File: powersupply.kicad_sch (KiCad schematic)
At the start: 33 parts, among them U2 MP28167GQ, U3 PAM2306AYPKE

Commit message: Label RasPi Zero W pin header
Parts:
- added D1: LED, LED_SMD:LED_0805_2012Metric, symbol Device:LED
- added J1: 2477, 2477, symbol STS1_EEE_lib:2477
- added R1: 220, Resistor_SMD:R_0603_1608Metric, symbol Device:R
- added SW1: SW_SPST, symbol Switch:SW_SPST
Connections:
- net AGND: now also D1.1 (K), J1.2 (-)
- net VBUS: now also R1.1, SW1.2 (B)
- new net: D1.2 (A), R1.2
- new net: J1.1 (+), SW1.1 (A)

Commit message: Add 3V3 LDO: could be used to set EPS_BAT_GOOD high
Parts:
- removed C17: 100n, Capacitor_SMD:C_0603_1608Metric_Pad1.08x0.95mm_HandSolder, symbol STS1_EDU-rescue:C-Device-STS1_template-rescue
- removed C18, C19, C20, C21: 10u, Capacitor_SMD:C_0603_1608Metric_Pad1.08x0.95mm_HandSolder, symbol STS1_EDU-rescue:C-Device-STS1_template-rescue
- removed L2, L3: 4.7uH, Inductor_SMD:L_1210_3225Metric_Pad1.42x2.65mm_HandSolder, symbol STS1_EDU-rescue:L-Device-STS1_template-rescue
- removed R13: 100k, Resistor_SMD:R_0603_1608Metric_Pad0.98x0.95mm_HandSolder, symbol STS1_EDU-rescue:R-Device-STS1_template-rescue
- removed TP1, TP2: TestPoint, TestPoint:TestPoint_Pad_1.0x1.0mm, symbol Connector:TestPoint
- removed U3: PAM2306AYPKE, PAM2306AYPKE:SON45P300X300X80-13N, symbol PAM2306AYPKE:PAM2306AYPKE
- added C13: 4.7u, Capacitor_SMD:C_0603_1608Metric, symbol Device:C
- added D23: PTVS3V3S1UR,115, Diode_SMD:D_SOD-123, symbol Device:D_Zener
- added U4: MCP1725-3302E_MC, STS1_3V3:MCP1725-3302E&slash_MC, symbol STS1_3V3:MCP1725-3302E_MC
- SW1: footprint (none) -> Button_Switch_THT:SW_DIP_SPSTx01_Slide_9.78x4.72mm_W7.62mm_P2.54mm
- renumbered C5 to C1, C14 to C10, C15 to C11, C16 to C12, C6 to C2, C7 to C3, C8 to C4, C9 to C5, C10 to C6, C11 to C7, C12 to C8, C13 to C9, D3 to D1, D4 to D2, D1 to D3, D5 to D4, D6 to D5, J1 to J3, R11 to R1, R12 to R2, R1 to R3, R14 to R4, R15 to R5, U2 to U3
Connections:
- net 3V3: now also C13.2, D23.1 (K), U4.7 (SENSE), U4.8 (VOUT)
- net AGND: now also C13.1, D23.2 (A), U4.4 (GND), U4.9 (EP)
- net VBUS: now also U4.1 (VIN), U4.2 (VIN), U4.3 (*SHDN)
- no-connect marks 0 -> 2
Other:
- note removed: "Step Down 5V --> 3V3 ^ 1V8"
- moved on the sheet: D3, J3, R3, SW1

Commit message: Clean-up
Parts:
- U4: footprint STS1_3V3:MCP1725-3302E&slash_MC -> STS_EEE:MCP1725-3302E&slash_MC
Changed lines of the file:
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@@
 			)
 		)
-		(property "Footprint" "STS1_3V3:MCP1725-3302E&slash_MC"
+		(property "Footprint" "STS_EEE:MCP1725-3302E&slash_MC"
 			(at 95.25 118.364 0)
 			(hide yes)

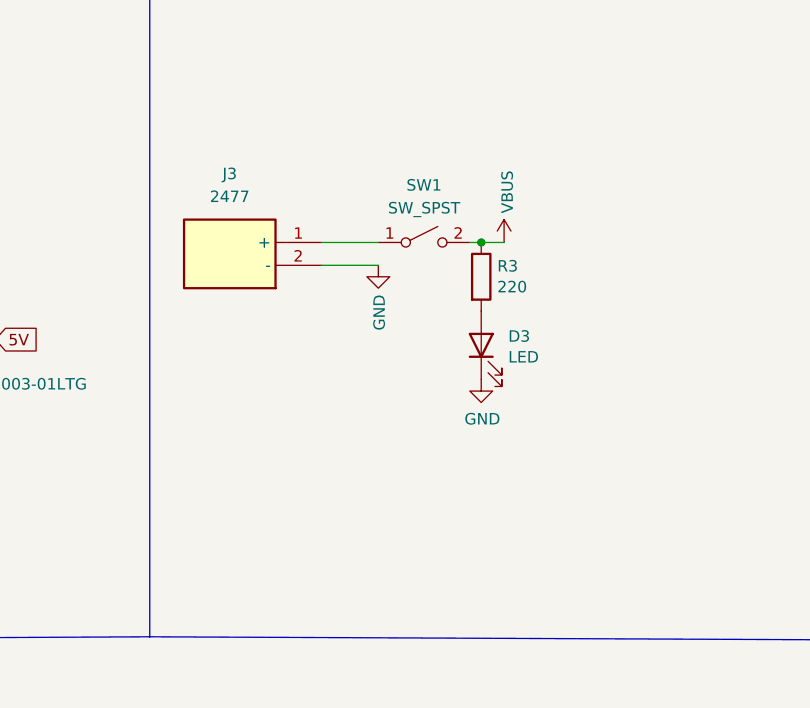
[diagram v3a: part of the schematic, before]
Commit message: Replace AA battery holder with 18650 one
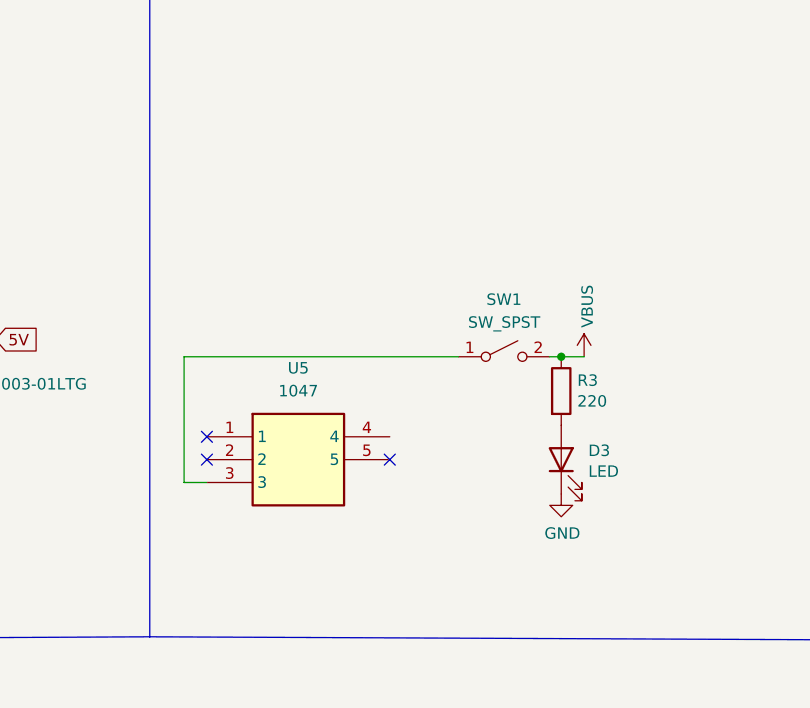
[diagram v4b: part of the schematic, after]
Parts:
- removed J3: 2477, 2477, symbol STS1_EEE_lib:2477
- added U5: 1047, 1047, symbol 1047:1047
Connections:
- net at SW1.1 (A): now also U5.3
- no-connect marks 2 -> 5
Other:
- moved on the sheet: D3, R3, SW1

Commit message: Position PiHat, Raspberry Zero, and battery holder
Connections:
- net 5V is gone; now on net VBUS: C10.1, C11.1, C12.1, C9.1, D2.1 (K), R5.1, U3.12 (OUT)
- net AGND: now also U5.4
- net VBUS: no longer C1.1, C2.1, C3.1, D1.1 (K), R1.1, R3.1, SW1.2 (B), U3.1 (IN)
- new net VBAT: C1.1, C2.1, C3.1, D1.1 (K), R1.1, R3.1, SW1.2 (B), U3.1 (IN)
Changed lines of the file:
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@@
 	(wire
 		(pts
+			(xy 294.64 64.77) (xy 289.56 64.77)
+		)
+		(stroke
+			(width 0)
+			(type default)
+		)
+	)
+	(wire
+		(pts
 			(xy 138.43 127) (xy 146.05 127)
 		)
@@
 	(wire
 		(pts
+			(xy 294.64 71.12) (xy 294.64 64.77)
+		)
+		(stroke
+			(width 0)
+			(type default)
+		)
+	)
+	(wire
+		(pts
 			(xy 120.65 127) (xy 123.19 127)
 		)
@@
 		)
 	)
-	(global_label "VBUS"
+	(global_label "VBAT"
 		(shape input)
 		(at 34.925 32.385 180)
@@
 		)
 		(property "Intersheetrefs" "${INTERSHEET_REFS}"
-			(at 27.7022 32.4644 0)
+			(at 28.1792 32.385 0)
 			(hide yes)
 			(show_name no)
@@
 		)
 	)
-	(global_label "5V"
+	(global_label "VBUS"
 		(shape input)
-		(at 389.255 106.68 90)
+		(at 63.5 124.46 180)
 		(fields_autoplaced yes)
 		(effects
@@
 				(size 1.27 1.27)
 			)
-			(justify left)
+			(justify right)
 		)
 		(property "Intersheetrefs" "${INTERSHEET_REFS}"
-			(at 389.1756 102.0577 90)
+			(at 56.2704 124.46 0)
 			(hide yes)
 			(show_name no)
@@
 					(size 1.27 1.27)
 				)
-				(justify left)
+				(justify right)
 			)
 		)
 	)
-	(global_label "3V3"
+	(global_label "VBUS"
 		(shape input)
-		(at 158.75 127 0)
+		(at 389.255 106.68 90)
 		(fields_autoplaced yes)
 		(effects
@@
 		)
 		(property "Intersheetrefs" "${INTERSHEET_REFS}"
-			(at 164.5886 127 0)
+			(at 389.255 99.4504 90)
 			(hide yes)
 			(show_name no)
@@
 		)
 	)
-	(global_label "5V"
+	(global_label "3V3"
 		(shape input)
-		(at 245.745 53.975 0)
+		(at 158.75 127 0)
 		(fields_autoplaced yes)
 		(effects
@@
 		)
 		(property "Intersheetrefs" "${INTERSHEET_REFS}"
-			(at 250.3673 53.8956 0)
+			(at 164.5886 127 0)
 			(hide yes)
 			(show_name no)
@@
 		)
 	)
-	(hierarchical_label "VBUS"
+	(global_label "VBUS"
 		(shape input)
-		(at 63.5 124.46 180)
+		(at 245.745 53.975 0)
+		(fields_autoplaced yes)
 		(effects
 			(font
 				(size 1.27 1.27)
 			)
-			(justify right)
+			(justify left)
+		)
+		(property "Intersheetrefs" "${INTERSHEET_REFS}"
+			(at 252.9746 53.975 0)
+			(hide yes)
+			(show_name no)
+			(do_not_autoplace no)
+			(effects
+				(font
+					(size 1.27 1.27)
+				)
+				(justify left)
+			)
 		)
 	)
@@
 	(symbol
 		(lib_id "power:GND")
+		(at 294.64 71.12 0)
+		(unit 1)
+		(body_style 1)
+		(exclude_from_sim no)
+		(in_bom yes)
+		(on_board yes)
+		(in_pos_files yes)
+		(dnp no)
+		(property "Reference" "#PWR053"
+			(at 294.64 77.47 0)
+			(hide yes)
+			(show_name no)
+			(do_not_autoplace no)
+			(effects
+				(font
+					(size 1.27 1.27)
+				)
+			)
+		)
+		(property "Value" "GND"
+			(at 294.767 75.5142 0)
+			(show_name no)
+			(do_not_autoplace no)
+			(effects
+				(font
+					(size 1.27 1.27)
+				)
+			)
+		)
+		(property "Footprint" ""
+			(at 294.64 71.12 0)
+			(hide yes)
+			(show_name no)
+			(do_not_autoplace no)
+			(effects
+				(font
+					(size 1.27 1.27)
+				)
+			)
+		)
+		(property "Datasheet" ""
+			(at 294.64 71.12 0)
+			(hide yes)
+			(show_name no)
+			(do_not_autoplace no)
+			(effects
+				(font
+					(size 1.27 1.27)
+				)
+			)
+		)
+		(property "Description" ""
+			(at 294.64 71.12 0)
+			(show_name no)
+			(do_not_autoplace no)
+			(effects
+				(font
+					(size 1.27 1.27)
+				)
+			)
+		)
+		(pin "1"
+		)
+		(instances
+			(project "STS1_EEE"
+				(path "/81e05c2b-9a2c-430f-84ee-6a59968cd49a/f7af00b0-76c3-459f-8c46-f5a83dd3bee8"
+					(reference "#PWR053")
+					(unit 1)
+				)
+			)
+		)
+	)
+	(symbol
+		(lib_id "power:GND")
 		(at 227.965 62.865 0)
 		(unit 1)
@@
 			)
 		)
-		(property "Value" "VBUS"
+		(property "Value" "VBAT"
 			(at 311.531 52.6542 90)
 			(show_name no)

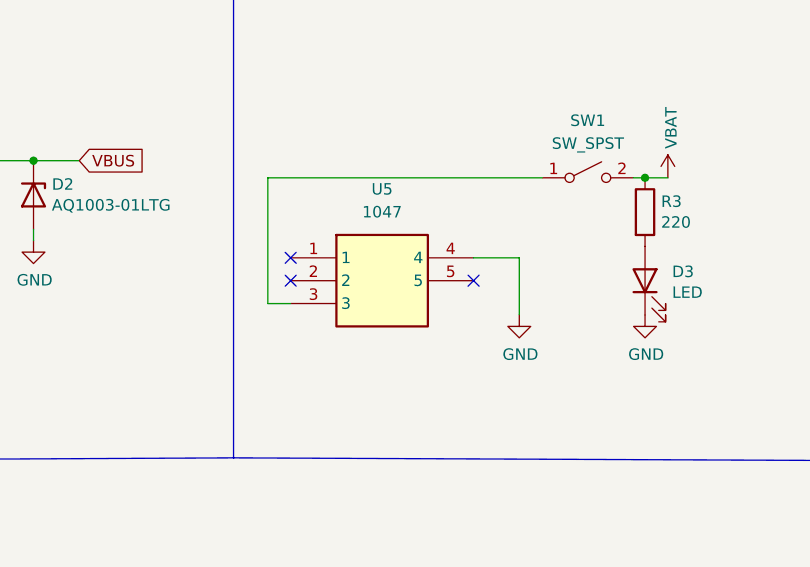
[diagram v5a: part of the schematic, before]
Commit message: Replace 1047 battery holder with 1048P (battery contacts connect to PCB using pads)
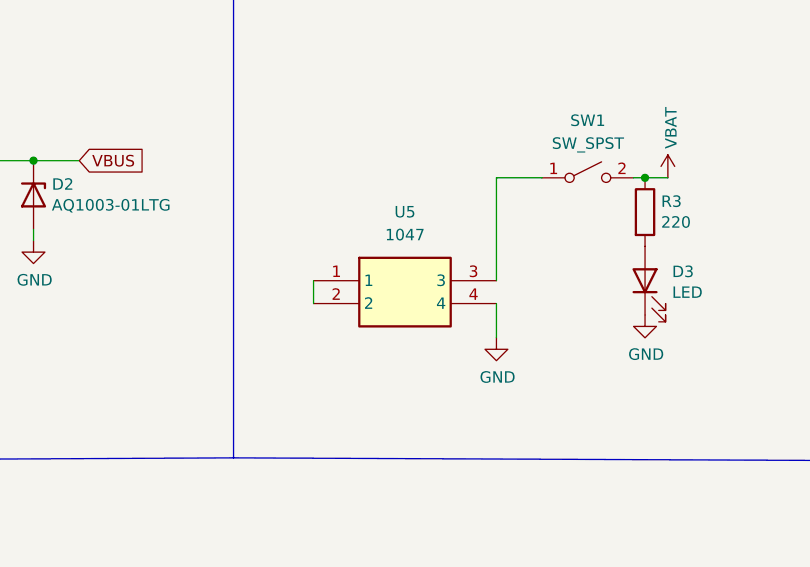
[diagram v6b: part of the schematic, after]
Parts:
- U5: footprint 1047 -> 1048P; symbol 1047:1047 -> STS1_EEE_lib:1048P; Manufacturer_Part_Number 1047 -> 1048P; Mouser Part Number 534-1047 -> 534-1048P; Mouser Price/Stock https://www.mouser.co.uk/ProductDetail/Keystone-Electronics/1047?qs=up89fPMRNqBQruBm7zqCRQ%3D%3D -> https://www.mouser.co.uk/ProductDetail/Keystone-Electronics/1048P?qs=9%252Bwcgl%2FJqd1h8Vx3IFpTxA%3D%3D
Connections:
- net at U5.1: now also U5.2
- no-connect marks 5 -> 2
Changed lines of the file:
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@@
 	)
 	(no_connect
-		(at 289.56 67.31)
-	)
-	(no_connect
 		(at 120.65 134.62)
 	)
 	(no_connect
-		(at 269.24 67.31)
-	)
-	(no_connect
 		(at 120.65 132.08)
 	)
-	(no_connect
-		(at 269.24 64.77)
-	)
 	(wire
 		(pts
@@
 	(wire
 		(pts
-			(xy 269.24 69.85) (xy 266.7 69.85)
-		)
-		(stroke
-			(width 0)
-			(type default)
-		)
-	)
-	(wire
-		(pts
 			(xy 205.105 62.865) (xy 205.105 61.595)
 		)
@@
 	(wire
 		(pts
-			(xy 266.7 55.88) (xy 297.18 55.88)
-		)
-		(stroke
-			(width 0)
-			(type default)
-		)
-	)
-	(wire
-		(pts
 			(xy 216.535 53.975) (xy 227.965 53.975)
 		)
@@
 	(wire
 		(pts
-			(xy 180.975 32.385) (xy 180.975 37.465)
+			(xy 292.1 69.85) (xy 292.1 73.66)
 		)
 		(stroke
@@
 	(wire
 		(pts
-			(xy 389.255 129.54) (xy 389.255 132.08)
+			(xy 180.975 32.385) (xy 180.975 37.465)
 		)
 		(stroke
@@
 	(wire
 		(pts
-			(xy 120.65 124.46) (xy 125.73 124.46)
+			(xy 389.255 129.54) (xy 389.255 132.08)
 		)
 		(stroke
@@
 	(wire
 		(pts
-			(xy 94.615 32.385) (xy 130.175 32.385)
+			(xy 120.65 124.46) (xy 125.73 124.46)
 		)
 		(stroke
@@
 	(wire
 		(pts
-			(xy 266.7 69.85) (xy 266.7 55.88)
+			(xy 94.615 32.385) (xy 130.175 32.385)
 		)
 		(stroke
@@
 	(wire
 		(pts
+			(xy 292.1 55.88) (xy 297.18 55.88)
+		)
+		(stroke
+			(width 0)
+			(type default)
+		)
+	)
+	(wire
+		(pts
 			(xy 63.5 124.46) (xy 67.31 124.46)
 		)
@@
 	(wire
 		(pts
+			(xy 292.1 55.88) (xy 292.1 67.31)
+		)
+		(stroke
+			(width 0)
+			(type default)
+		)
+	)
+	(wire
+		(pts
 			(xy 120.015 46.355) (xy 130.175 46.355)
 		)
@@
 	(wire
 		(pts
-			(xy 294.64 64.77) (xy 289.56 64.77)
+			(xy 138.43 127) (xy 146.05 127)
 		)
 		(stroke
@@
 	(wire
 		(pts
-			(xy 138.43 127) (xy 146.05 127)
+			(xy 170.815 37.465) (xy 180.975 37.465)
 		)
 		(stroke
@@
 	(wire
 		(pts
-			(xy 170.815 37.465) (xy 180.975 37.465)
+			(xy 307.34 55.88) (xy 308.61 55.88)
 		)
 		(stroke
@@
 	(wire
 		(pts
-			(xy 307.34 55.88) (xy 308.61 55.88)
+			(xy 130.175 67.945) (xy 130.175 59.055)
 		)
 		(stroke
@@
 	(wire
 		(pts
-			(xy 130.175 67.945) (xy 130.175 59.055)
+			(xy 216.535 62.865) (xy 216.535 61.595)
 		)
 		(stroke
@@
 	(wire
 		(pts
-			(xy 216.535 62.865) (xy 216.535 61.595)
+			(xy 170.815 60.325) (xy 170.815 62.865)
 		)
 		(stroke
@@
 	(wire
 		(pts
-			(xy 170.815 60.325) (xy 170.815 62.865)
+			(xy 271.78 67.31) (xy 271.78 69.85)
 		)
 		(stroke
@@
 	(wire
 		(pts
-			(xy 294.64 71.12) (xy 294.64 64.77)
-		)
-		(stroke
-			(width 0)
-			(type default)
-		)
-	)
-	(wire
-		(pts
 			(xy 120.65 127) (xy 123.19 127)
 		)
@@
 	(symbol
 		(lib_id "power:GND")
-		(at 294.64 71.12 0)
+		(at 292.1 73.66 0)
 		(unit 1)
 		(body_style 1)
@@
 		(dnp no)
 		(property "Reference" "#PWR053"
-			(at 294.64 77.47 0)
+			(at 292.1 80.01 0)
 			(hide yes)
 			(show_name no)
@@
 		)
 		(property "Value" "GND"
-			(at 294.767 75.5142 0)
+			(at 292.227 78.0542 0)
 			(show_name no)
 			(do_not_autoplace no)
@@
 		)
 		(property "Footprint" ""
-			(at 294.64 71.12 0)
+			(at 292.1 73.66 0)
 			(hide yes)
 			(show_name no)
@@
 		)
 		(property "Datasheet" ""
-			(at 294.64 71.12 0)
+			(at 292.1 73.66 0)
 			(hide yes)
 			(show_name no)
@@
 		)
 		(property "Description" ""
-			(at 294.64 71.12 0)
+			(at 292.1 73.66 0)
 			(show_name no)
 			(do_not_autoplace no)
@@
 	)
 	(symbol
-		(lib_id "1047:1047")
-		(at 269.24 64.77 0)
+		(lib_id "STS1_EEE_lib:1048P")
+		(at 271.78 67.31 0)
 		(unit 1)
 		(body_style 1)
@@
 		(fields_autoplaced yes)
 		(property "Reference" "U5"
-			(at 279.4 57.15 0)
+			(at 281.94 59.69 0)
 			(show_name no)
 			(do_not_autoplace no)
@@
 		)
 		(property "Value" "1047"
-			(at 279.4 59.69 0)
+			(at 281.94 62.23 0)
 			(show_name no)
 			(do_not_autoplace no)
@@
 			)
 		)
-		(property "Footprint" "1047"
-			(at 285.75 159.69 0)
+		(property "Footprint" "1048P"
+			(at 288.29 162.23 0)
 			(hide yes)
 			(show_name no)
@@
 			)
 		)
-		(property "Datasheet" "https://www.keyelco.com/product.cfm/product_id/14061"
-			(at 285.75 259.69 0)
+		(property "Datasheet" "http://www.keyelco.com/product-pdf.cfm?p=13959"
+			(at 288.29 262.23 0)
 			(hide yes)
 			(show_name no)
@@
 			)
 		)
-		(property "Description" "KEYSTONE - 1047 - BATTERY HOLDER, 18650 LI-ION, 2CELL, PCB"
-			(at 269.24 64.77 0)
+		(property "Description" "KEYSTONE - 1048P - BATTERY HOLDER, 18650, SMD"
+			(at 271.78 67.31 0)
 			(hide yes)
 			(show_name no)
@@
 		)
 		(property "Height" "14.85"
-			(at 285.75 459.69 0)
+			(at 288.29 462.23 0)
 			(hide yes)
 			(show_name no)
@@
 			)
 		)
-		(property "Mouser Part Number" "534-1047"
-			(at 285.75 559.69 0)
+		(property "Mouser Part Number" "534-1048P"
+			(at 288.29 562.23 0)
 			(hide yes)
 			(show_name no)
@@
 			)
 		)
-		(property "Mouser Price/Stock" "https://www.mouser.co.uk/ProductDetail/Keystone-Electronics/1047?qs=up89fPMRNqBQruBm7zqCRQ%3D%3D"
-			(at 285.75 659.69 0)
+		(property "Mouser Price/Stock" "https://www.mouser.co.uk/ProductDetail/Keystone-Electronics/1048P?qs=9%252Bwcgl%2FJqd1h8Vx3IFpTxA%3D%3D"
+			(at 288.29 662.23 0)
 			(hide yes)
 			(show_name no)
@@
 		)
 		(property "Manufacturer_Name" "Keystone Electronics"
-			(at 285.75 759.69 0)
+			(at 288.29 762.23 0)
 			(hide yes)
 			(show_name no)
@@
 			)
 		)
-		(property "Manufacturer_Part_Number" "1047"
-			(at 285.75 859.69 0)
+		(property "Manufacturer_Part_Number" "1048P"
+			(at 288.29 862.23 0)
 			(hide yes)
 			(show_name no)
@@
 			)
 		)
-		(pin "5"
-		)
 		(pin "4"

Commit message: Finilize connection and placement of components
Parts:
- removed C13: 4.7u, Capacitor_SMD:C_0603_1608Metric, symbol Device:C
- removed D23: PTVS3V3S1UR,115, Diode_SMD:D_SOD-123, symbol Device:D_Zener
- removed D3: LED, LED_SMD:LED_0805_2012Metric, symbol Device:LED
- removed R3: 220, Resistor_SMD:R_0603_1608Metric, symbol Device:R
- removed U4: MCP1725-3302E_MC, STS_EEE:MCP1725-3302E&slash_MC, symbol STS1_3V3:MCP1725-3302E_MC
- U4: renamed from U5; footprint 1048P -> STS_EEE:1048P
- renumbered D4 to D3, D5 to D4, R4 to R3, R5 to R4
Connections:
- net 3V3 renamed Pi_3V3
- no-connect marks 2 -> 0
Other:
- note added: "Battery power switch"
- note added: "Step Down VBAT --> VBUS 5V"
- note removed: "Step Down VBUS --> 5V"
- moved on the sheet: D3, D4, R3, R4, SW1, U4

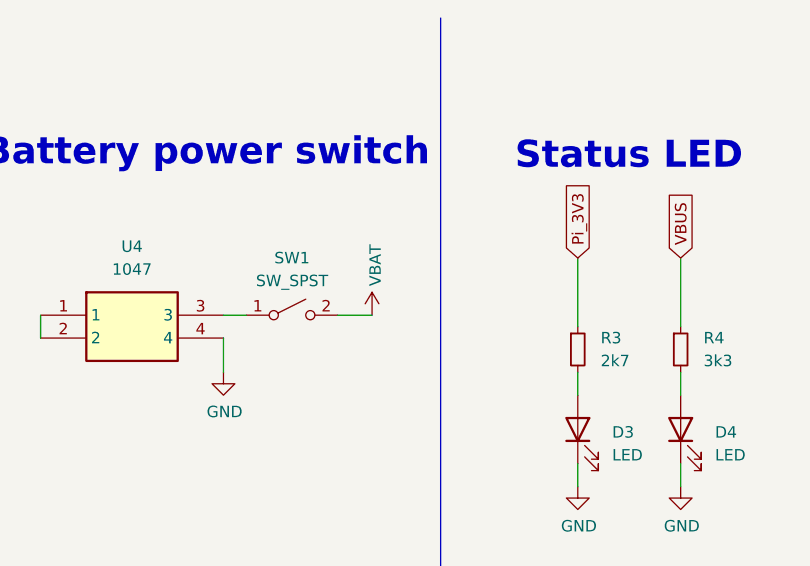
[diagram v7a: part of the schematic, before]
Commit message: Fix ERC errors
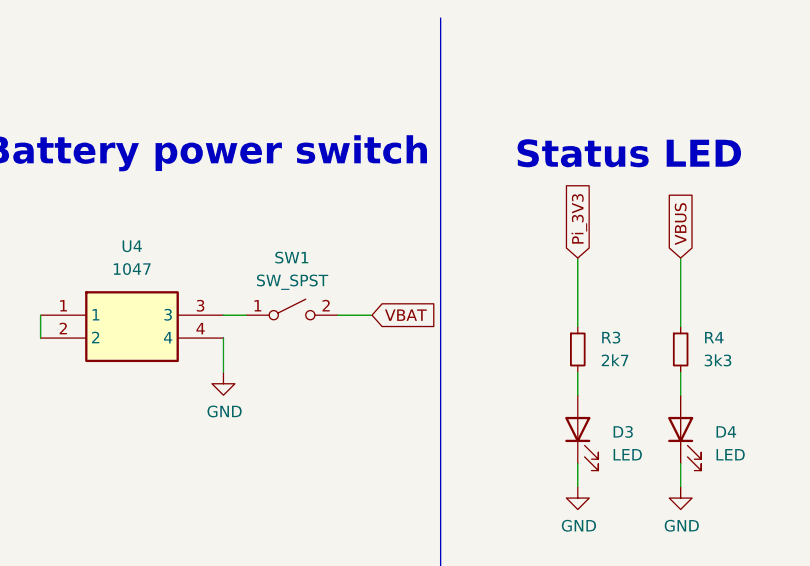
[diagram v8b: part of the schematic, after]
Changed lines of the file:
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@@
 		)
 	)
+	(global_label "VBAT"
+		(shape input)
+		(at 309.88 45.72 0)
+		(fields_autoplaced yes)
+		(effects
+			(font
+				(size 1.27 1.27)
+			)
+			(justify left)
+		)
+		(property "Intersheetrefs" "${INTERSHEET_REFS}"
+			(at 316.6258 45.72 0)
+			(hide yes)
+			(show_name no)
+			(do_not_autoplace no)
+			(effects
+				(font
+					(size 1.27 1.27)
+				)
+				(justify left)
+			)
+		)
+	)
 	(global_label "VBUS"
 		(shape input)
@@
 					(unit 1)
 				)
-			)
-		)
-	)
-	(symbol
-		(lib_id "power:VBUS")
-		(at 309.88 45.72 0)
-		(unit 1)
-		(body_style 1)
-		(exclude_from_sim no)
-		(in_bom yes)
-		(on_board yes)
-		(in_pos_files yes)
-		(dnp no)
-		(property "Reference" "#PWR048"
-			(at 309.88 49.53 0)
-			(hide yes)
-			(show_name no)
-			(do_not_autoplace no)
-			(effects
-				(font
-					(size 1.27 1.27)
-				)
-			)
-		)
-		(property "Value" "VBAT"
-			(at 310.261 42.4942 90)
-			(show_name no)
-			(do_not_autoplace no)
-			(effects
-				(font
-					(size 1.27 1.27)
-				)
-				(justify left)
-			)
-		)
-		(property "Footprint" ""
-			(at 309.88 45.72 0)
-			(hide yes)
-			(show_name no)
-			(do_not_autoplace no)
-			(effects
-				(font
-					(size 1.27 1.27)
-				)
-			)
-		)
-		(property "Datasheet" ""
-			(at 309.88 45.72 0)
-			(hide yes)
-			(show_name no)
-			(do_not_autoplace no)
-			(effects
-				(font
-					(size 1.27 1.27)
-				)
-			)
-		)
-		(property "Description" ""
-			(at 309.88 45.72 0)
-			(show_name no)
-			(do_not_autoplace no)
-			(effects
-				(font
-					(size 1.27 1.27)
-				)
-			)
-		)
-		(pin "1"
-		)
-		(instances
-			(project "STS1_EEE"
-				(path "/81e05c2b-9a2c-430f-84ee-6a59968cd49a/f7af00b0-76c3-459f-8c46-f5a83dd3bee8"
-					(reference "#PWR048")
-					(unit 1)
-				)
